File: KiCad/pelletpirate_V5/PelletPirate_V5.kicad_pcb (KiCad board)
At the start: 2 copper layers, 65 x 110 mm, 134 parts, among them J1 SJ1-3523NG_Jack_PP, J10 TB002-500-02BE, J2 SJ1-3523NG_Jack_PP, J3 SJ1-3523NG_Jack_PP, J4 SJ1-3523NG_Jack_PP, J5 SJ1-3523NG_Jack_PP, J6 Conn_01x04, J7 Conn_01x04_Socket, J9 USB4145-03-0070-C_REVA2, T1 BTA12-Triac, T2 BTA12-Triac, T3 BTA12-600BWRG, U1 USBLC6-2SC6, U3 H11AA1M

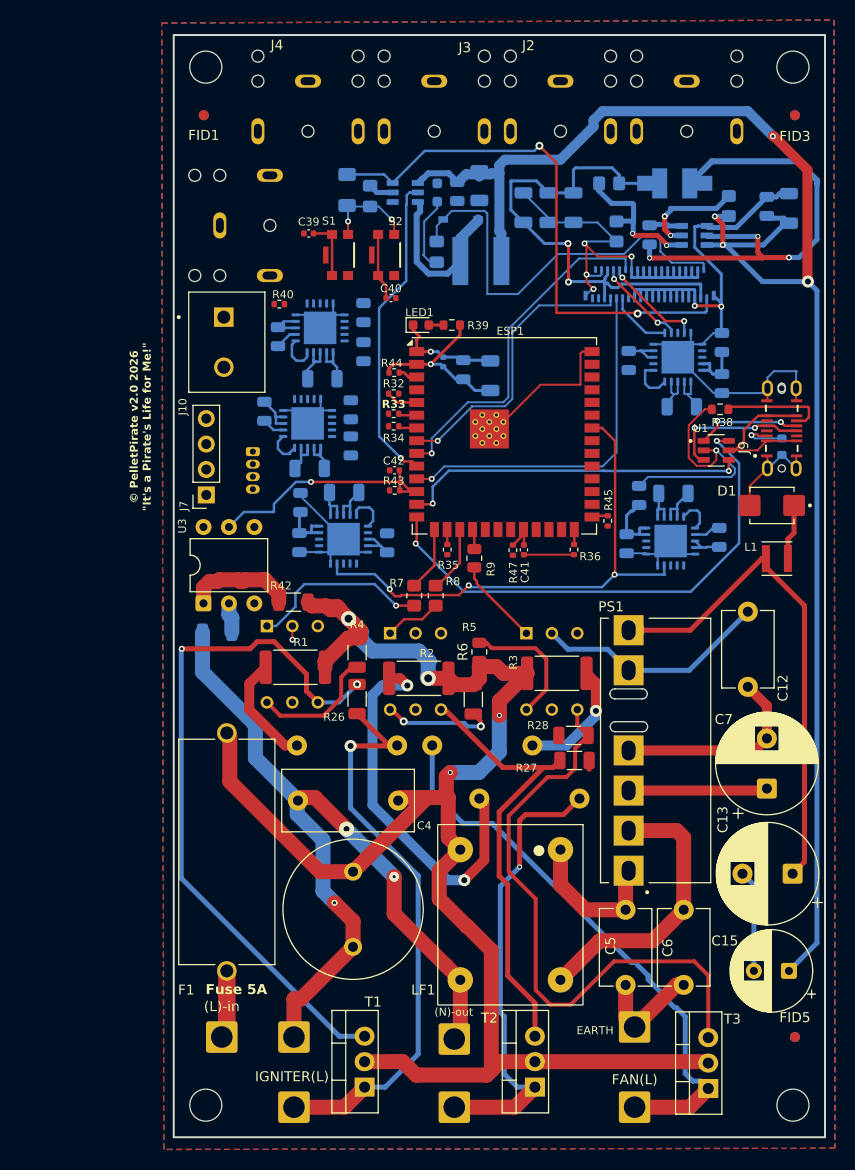
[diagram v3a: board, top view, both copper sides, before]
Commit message: V5 DRC Clean / ERC Clean
USB-C corner closed out:
- USB4145 footprint copper verified against GCT drawing (unproven-source flag retired)
- Per-pad solder mask expansion zeroed -> real 0.2mm mask dams (10 aperture-bridge DRC cleared)
- Hidden power-in duplicate pins (A9/A12/B9/B12) converted to hidden passive (shield-pin style); implicit VBUS_A/GND_A global net injection eliminated
- Net renamed VBUS_A -> /VBUS; USB netclass pattern fixed to /VBUS (silent class dropout repaired)
- ERC 0/0 verified via kicad-cli at all severities; DRC clean with fresh zone fills
- Top-half placement plan sketch added (MAX tiles under jacks, ESP south, U3 east, PS3 to FPC backlight end)

Co-Authored-By: Claude Fable 5 <noreply@anthropic.com>
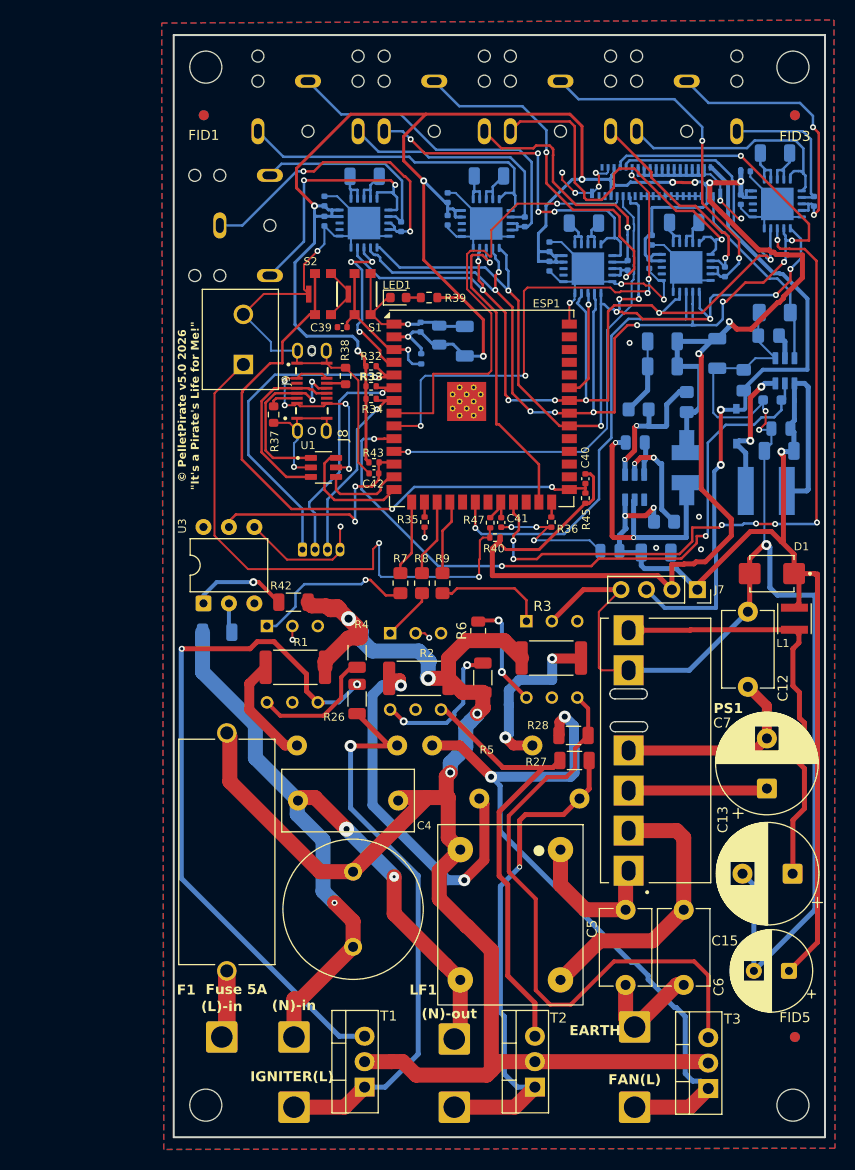
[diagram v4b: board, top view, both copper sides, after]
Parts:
- C21, C22, C23, C24, C25, C26, C27, C28, C29, C30, C31, C32, C33, C34, C35: footprint Capacitor_SMD:C_0805_2012Metric -> Capacitor_SMD:C_0402_1005Metric
- D2: footprint STPS0540Z_Schotty Diode LED:SOD-123 -> STPS0540Z_Schotty Diode LED:D2-Footprint-Flyman
- R37: moved to F.Cu
- R44: moved to B.Cu
- R9: footprint Resistor_SMD:R_0805_2012Metric -> Resistor_SMD:R_0805_2012Metric_Pad1.20x1.40mm_HandSolder
- WirePad2: value NEUTRAL-In -> (N)-in
- moved C30 55.2 mm to (183.9, 56.6), turned to 90 degrees
- moved R37 50.8 mm to (130.0, 77.9)
- moved R25 50.5 mm to (180.0, 51.8), turned to 0 degrees
- moved J7 49.9 mm to (172.3, 95.3), turned to -90 degrees
- moved J1 48.8 mm to (124.6, 59.0), turned to 0 degrees
- moved J5 48.8 mm to (171.2, 44.6), turned to -90 degrees
- moved C29 48.0 mm to (175.0, 63.6), turned to 90 degrees
- moved MAX5 47.3 mm to (180.2, 56.9), turned to -90 degrees
- moved J8 47.0 mm to (133.8, 75.5)
- moved R24 44.7 mm to (170.9, 58.7), turned to 0 degrees
- moved R17 44.4 mm to (180.0, 67.7), turned to 180 degrees
- moved C35 42.2 mm to (177.1, 53.6), turned to 180 degrees
- moved C36 42.1 mm to (179.4, 70.0), turned to 180 degrees
- moved PS3 41.9 mm to (181.0, 73.5), turned to 90 degrees
- moved MAX4 40.9 mm to (171.2, 63.2), turned to -90 degrees
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- renumbered J9 to J8, J10 to J9
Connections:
- net VBUS_A renamed /VBUS
- C11 pad 1: GND -> +12V
- C11 pad 2: +12V -> GND
- ESP1 pad 23: /MAX1_CS -> /MAX5_CS
- ESP1 pad 4: /MAX5_CS -> /MAX1_CS
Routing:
- net +3.3V: track 85.7 -> 303.6 mm, vias 3 -> 12
- net /ALL_SCLK: track 9.11 -> 115.5 mm, vias 2 -> 10
- net GND: track 274.3 -> 373.8 mm, vias 11 -> 26
- net /ALL_SDI: track 6.29 -> 98.5 mm, vias 0 -> 8
- net /MAX5_CS: track 0.00 -> 71.3 mm, vias 0 -> 7
- net Net-(J9-Pad1): track 0.00 -> 57.3 mm, vias 0 -> 2
- net +12V: track 169.2 -> 114.7 mm, vias 4 -> 3
- net Net-(ESP1-IO0): track 8.30 -> 61.0 mm, vias 0 -> 2
- net /ALL_SDO: track 63.1 -> 109.0 mm, vias 5 -> 7
- net /MAX4_CS: track 0.00 -> 44.3 mm, vias 0 -> 1
- net /USB_D+: track 51.3 -> 11.8 mm, vias 2 -> 0
- net /LED_PWM: track 31.4 -> 68.3 mm, vias 1 -> 3
- net /LED-: track 54.9 -> 20.1 mm, vias 2 -> 0
- net Net-(J4-Ring): track 3.65 -> 37.8 mm, vias 0 -> 1
- net Net-(J3-Sleeve): track 4.05 -> 38.0 mm, vias 0 -> 2
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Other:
- board text added: "© PelletPirate v5.0 2026 {dblquote}It's a Pirate's Life for Me!{dblquote}"
- board text removed: "3053"
- board text removed: "© PelletPirate v2.0 2026 {dblquote}It's a Pirate's Life for Me!{dblquote}"

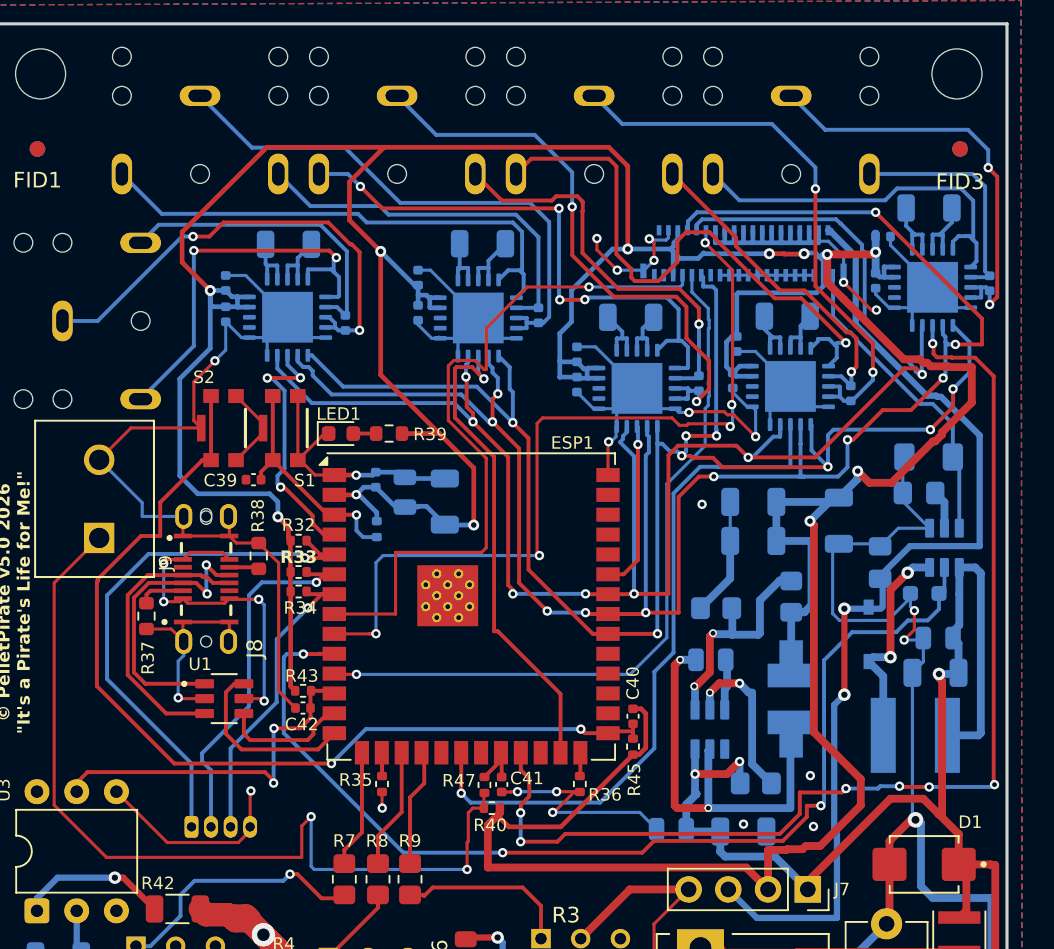
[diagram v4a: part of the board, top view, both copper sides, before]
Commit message: V5 pre-library-localization safety checkpoint
- Audit remediation complete: corridor items 1-5 + 7 closed (LED/SPI reroute,
  J4 overlays, CS nudges, MAX5_CS old run deleted, ZC_DET+GND test points TP1/TP2,
  parity field sync). ERC 0/0, DRC 0/0, parity 0.
- New-connector audit: J8 USB4145 + J9 TB002 verified against datasheets;
  finding F1 open (stake variant 0070 -> 0170 swap pending)
- USB_try2: staged 0170 symbol (hidden-pin-fixed) + footprint + STEP
- V5_Library_Localization_Plan.md: proposed plan, not yet executed

Co-Authored-By: Claude Fable 5 <noreply@anthropic.com>
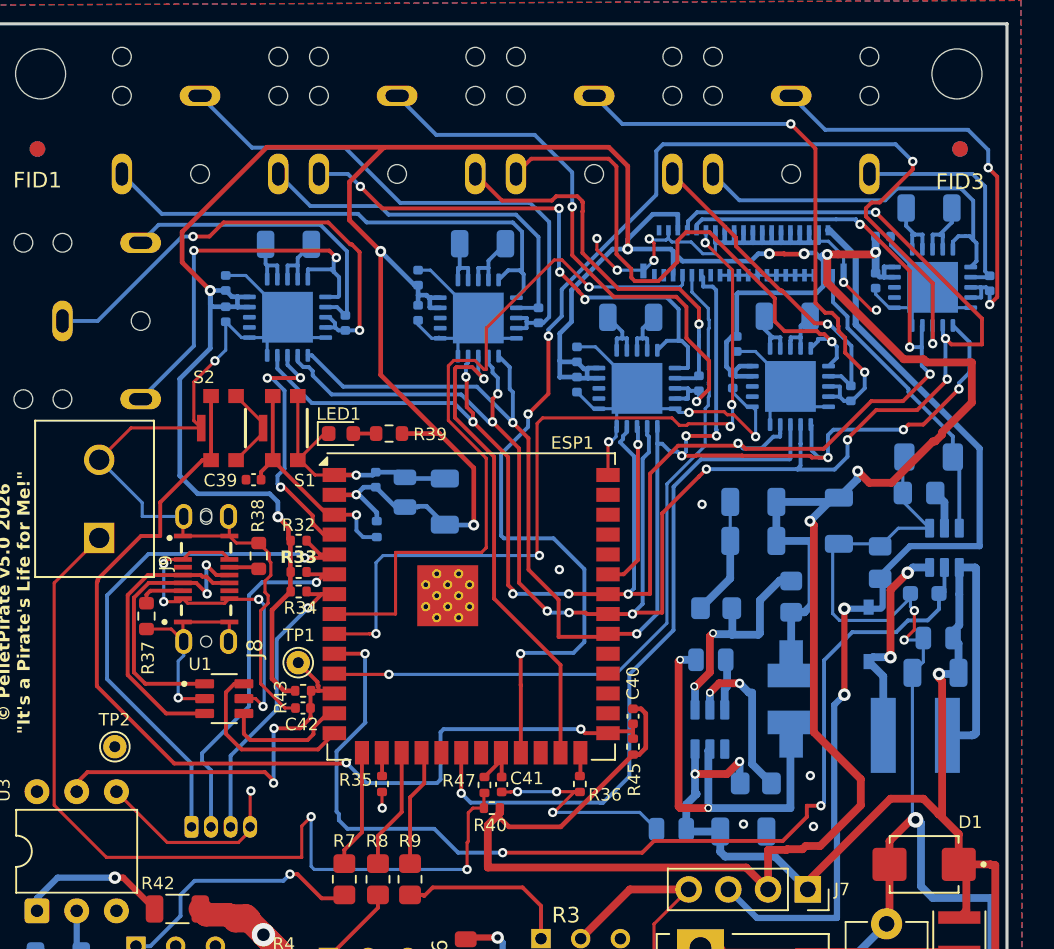
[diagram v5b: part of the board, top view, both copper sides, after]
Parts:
- added TP1: TestPoint, TestPoint:TestPoint_THTPad_D1.5mm_Drill0.7mm, F.Cu at (139.7, 80.8)
- added TP2: TestPoint, TestPoint:TestPoint_THTPad_D1.5mm_Drill0.7mm, F.Cu at (128.0, 86.2)
- J8: value USB4145-03-0070-C_REVA2 -> USB4145-03-0170-C
- T1, T2: value BTA12-Triac -> BTA12-600BWRG
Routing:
- net /MAX5_CS: track 71.3 -> 83.5 mm, vias 7 -> 5
- net GND: track 373.8 -> 380.3 mm, vias 26 -> 27
- net +3.3V: track 303.6 -> 309.2 mm
- net Net-(ESP1-IO0): track 61.0 -> 63.8 mm
- net /ZC_DET: track 23.3 -> 25.7 mm
- net /LCD_RST: track 46.2 -> 47.6 mm
- net Net-(J3-Ring): track 36.8 -> 35.8 mm
- net Net-(J4-Ring): track 37.8 -> 37.0 mm
- net /ALL_SDI: track 98.5 -> 97.7 mm
- net /LED+: track 64.5 -> 63.8 mm
- net Net-(J4-Tip): track 21.3 -> 20.6 mm
- net /ALL_SCLK: track 115.5 -> 114.9 mm
- net /LED_PWM: track 68.3 -> 67.7 mm
- net /LCD_DC: track 47.1 -> 46.6 mm
- net /LED-: track 20.1 -> 19.6 mm
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
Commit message: V5 pre-BOM-fill checkpoint: J8 0170 swap in sch+board, footprint/mask cleanups, BOM fill table
Co-Authored-By: Claude Fable 5 <noreply@anthropic.com>
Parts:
- J8: footprint USB_try2:GCT_USB4145-03-0070-C_REVA2 -> USB_try2:GCT_USB4145-03-0170-C
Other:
- board text added: "+12V"
- board text added: "+3.3V"
- board text added: "3053M"
- board text added: "GND"
- board text added: "LED+"
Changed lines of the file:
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@@
 		(property "Value" "AUGER(L)"
 			(at 0 -3 0)
-			(layer "F.Fab")
+			(layer "F.SilkS")
 			(effects
 				(font
@@
 		(tags "resistor")
 		(property "Reference" "R2"
-			(at -0.8 2.5 0)
+			(at -0.0375 2.5 0)
 			(layer "F.SilkS")
 			(effects
@@
 		(tags "CP Radial series Radial pin pitch 5.00mm diameter 10mm height 16mm Electrolytic Capacitor")
 		(property "Reference" "C13"
-			(at 6.967677 5.4 90)
+			(at -1.457323 4.925 0)
 			(layer "F.SilkS")
 			(effects
@@
 		(at 126.95 72.875 90)
 		(property "Reference" "J9"
-			(at -1.6 4.25 90)
+			(at -3.25 -3.55 90)
 			(layer "F.SilkS")
 			(effects
@@
 		(tags "C Rect series Radial pin pitch 10.00mm length 13mm width 6mm Capacitor")
 		(property "Reference" "C4"
-			(at -2.6 -2.5 180)
+			(at -2.6 2.525 180)
 			(layer "F.SilkS")
 			(effects
@@
 		(tags "resistor")
 		(property "Reference" "R5"
-			(at 7.2 -0.4 0)
+			(at 1.8625 -1.875 0)
 			(layer "F.SilkS")
 			(effects
@@
 		)
 		(property "Value" "EARTH"
-			(at -3.95 0.35 0)
+			(at -3.125 -0.05 90)
 			(layer "F.SilkS")
 			(effects
@@
 		(tags "C Disc series Radial pin pitch 7.50mm diameter 7.5mm width 5.0mm Capacitor")
 		(property "Reference" "C5"
-			(at 1.9 3.35 90)
+			(at -0.775 1.975 0)
 			(layer "F.SilkS")
 			(effects
@@
 		(tags "C Disc series Radial pin pitch 7.50mm diameter 7.5mm width 5.0mm Capacitor")
 		(property "Reference" "C6"
-			(at 7.7 -3.5 90)
+			(at -0.75 1.875 0)
 			(layer "F.SilkS")
 			(effects
@@
 		(at 125.3 121.525 90)
 		(property "Reference" "F1"
-			(at -13.775 -4.05 0)
+			(at 12.275 -3 0)
 			(layer "F.SilkS")
 			(effects
@@
 		(tags "fiducial")
 		(property "Reference" "FID5"
-			(at 0 -1.95 0)
+			(at 0.225 -1.825 0)
 			(layer "F.SilkS")
 			(effects
@@
 		(tags "CP Radial series Radial pin pitch 3.50mm diameter 8mm height 12mm Electrolytic Capacitor")
 		(property "Reference" "C15"
-			(at 6.4 3 0)
+			(at 6.075 3.5 0)
 			(layer "F.SilkS")
 			(effects
@@
 		(tags "resistor")
 		(property "Reference" "R1"
-			(at -0.5375 2.5 0)
+			(at -0.8125 2.5 0)
 			(layer "F.SilkS")
 			(effects
@@
 		(tags "resistor")
 		(property "Reference" "R37"
-			(at 2.675 -0.1 270)
+			(at -0.2 1.245 270)
 			(layer "F.SilkS")
 			(effects
@@
 		)
 	)
-	(footprint "USB_try2:GCT_USB4145-03-0070-C_REVA2"
+	(footprint "USB_try2:GCT_USB4145-03-0170-C"
 		(layer "F.Cu")
 		(at 133.785 75.5 90)
 		(property "Reference" "J8"
-			(at -4.45 3.115 90)
+			(at -4.75 -2.885 90)
 			(layer "F.SilkS")
 			(effects
@@
 		(sheetname "/")
 		(sheetfile "PelletPirate_V5.kicad_sch")
-		(units
-			(unit
-				(name "A")
-				(pins "A4" "A9" "A5" "A6" "A7" "A8" "A1" "A12" "S1" "S2" "S3" "S4" "B4"
-					"B9" "B8" "B7" "B6" "B5" "B1" "B12"
-				)
-			)
-		)
 		(attr smd)
 		(duplicate_pad_numbers_are_jumpers no)
@@
 		)
 		(embedded_fonts no)
-		(model "${KIPRJMOD}/USB_try2/usb4145-03-0070-c.stp"
-			(hide yes)
-			(offset
-				(xyz 0 -1.3 -0.11)
-			)
-			(scale
-				(xyz 1 1 1)
-			)
-			(rotate
-				(xyz -90 -0 -0)
-			)
-		)
-		(model "${KIPRJMOD}/USB_try2/usb4145-03-0170-c.stp"
-			(offset
-				(xyz 0 -1.35 -0.12)
-			)
-			(scale
-				(xyz 1 1 1)
-			)
-			(rotate
-				(xyz -90 -0 -0)
-			)
-		)
 	)
 	(footprint "Capacitor_SMD:C_0402_1005Metric"
@@
 		(at 137.9 123.5 -90)
 		(property "Reference" "MOV1"
-			(at 0 -0.5 270)
+			(at -2.525 -5.925 0)
 			(unlocked yes)
 			(layer "F.SilkS")
-			(hide yes)
 			(effects
 				(font
-					(size 1 1)
+					(size 0.8 0.8)
 					(thickness 0.1)
 				)
@@
 		)
 		(fp_text user "${REFERENCE}"
-			(at 3.75 -3 0)
+			(at -1.45 -0.175 0)
 			(unlocked yes)
 			(layer "F.Fab")
@@
 		(tags "resistor")
 		(property "Reference" "R28"
-			(at 3.55 1 0)
+			(at -1.075 1.7 0)
 			(layer "F.SilkS")
 			(effects
@@
 		(tags "CP Radial series Radial pin pitch 5.00mm diameter 10mm height 16mm Electrolytic Capacitor")
 		(property "Reference" "C7"
-			(at 6.55 -4.45 0)
+			(at 7.325 3.8 0)
 			(layer "F.SilkS")
 			(effects
@@
 			(at 0 -1.83 0)
 			(layer "B.Fab")
+			(hide yes)
 			(effects
 				(font
@@
 		(at 131.84 102.79 -90)
 		(property "Reference" "MOC1"
-			(at -5.24 -4.31 0)
+			(at -5.24 0.79 0)
 			(layer "B.SilkS")
 			(effects
@@
 		)
 		(property "Value" "MOC3063M"
-			(at 0.01 -0.34 90)
+			(at 0.01 -0.035 0)
 			(layer "B.Fab")
 			(effects
@@
 			(at 0 -1.83 0)
 			(layer "B.Fab")
+			(hide yes)
 			(effects
 				(font
@@
 		(tags "fiducial")
 		(property "Reference" "FID6"
-			(at 0 1.95 0)
+			(at -0.225 1.825 0)
 			(layer "B.SilkS")
 			(effects
@@
 		(at 144.14 103.51 -90)
 		(property "Reference" "MOC2"
-			(at -5.21 -2.81 0)
+			(at -5.21 0.665 0)
 			(layer "B.SilkS")
 			(effects
@@
 		)
 		(property "Value" "MOC3063M"
-			(at -0.21 0.36 90)
+			(at -1.11 0.015 0)
 			(layer "B.Fab")
 			(effects
@@
 			(at 0 -1.83 0)
 			(layer "B.Fab")
+			(hide yes)
 			(effects
 				(font
@@
 		(at 157.74 102.31 -90)
 		(property "Reference" "MOC3"
-			(at -5.36 -2.91 0)
+			(at -5.31 4.515 0)
 			(layer "B.SilkS")
 			(effects
@@
 		)
 		(property "Value" "MOC3053M"
-			(at 9.921 -5.395 90)
+			(at -1.51 0.115 0)
 			(layer "B.Fab")
 			(effects
@@
 			(at 0 -1.83 180)
 			(layer "B.Fab")
+			(hide yes)
 			(effects
 				(font
@@
 			(at 0 -1.83 0)
 			(layer "B.Fab")
+			(hide yes)
 			(effects
 				(font
@@
 			(at 0 -1.16 90)
 			(layer "B.Fab")
+			(hide yes)
 			(effects
 				(font
@@
 		(layer "Edge.Cuts")
 	)
+	(gr_text "GND"
+		(at 165.15 93.525 90)
+		(layer "F.SilkS")
+		(effects
+			(font
+				(size 0.8 0.8)
+				(thickness 0.16)
+				(bold yes)
+			)
+			(justify left bottom)
+		)
+	)
+	(gr_text "LED+"
+		(at 167.675 93.525 90)
+		(layer "F.SilkS")
+		(effects
+			(font
+				(size 0.8 0.8)
+				(thickness 0.16)
+				(bold yes)
+			)
+			(justify left bottom)
+		)
+	)
+	(gr_text "+3.3V"
+		(at 170.175 93.525 90)
+		(layer "F.SilkS")
+		(effects
+			(font
+				(size 0.8 0.8)
+				(thickness 0.16)
+				(bold yes)
+			)
+			(justify left bottom)
+		)
+	)
+	(gr_text "+12V"
+		(at 172.7 93.525 90)
+		(layer "F.SilkS")
+		(effects
+			(font
+				(size 0.8 0.8)
+				(thickness 0.16)
+				(bold yes)
+			)
+			(justify left bottom)
+		)
+	)
 	(gr_text "© PelletPirate v5.0 2026\n{dblquote}It's a Pirate's Life for Me!{dblquote}"
 		(at 122.6 77 90)
@@
 		)
 	)
+	(gr_text "3053M"
+		(at 160.9 97.425 0)
+		(layer "B.SilkS")
+		(effects
+			(font
+				(size 0.8 0.8)
+				(thickness 0.2)
+				(bold yes)
+			)
+			(justify left bottom mirror)
+		)
+	)

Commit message: V5 field sync to board complete: ERC 0 / DRC 0 / parity 0
BOM fields (MF/MP/LINK on 35 parts) synced sch->pcb via Update-PCB.
Board and schematic fully consistent. BOM: 117 rows, 59 unique MPNs, no gaps.

Co-Authored-By: Claude Fable 5 <noreply@anthropic.com>
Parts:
- R6: value 180Ω -> 180Ω
